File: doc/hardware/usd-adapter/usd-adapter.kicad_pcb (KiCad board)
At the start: 2 copper layers, 14.2 x 25 mm, 2 parts, among them J1 usd-plug, P1 CONN_02X04

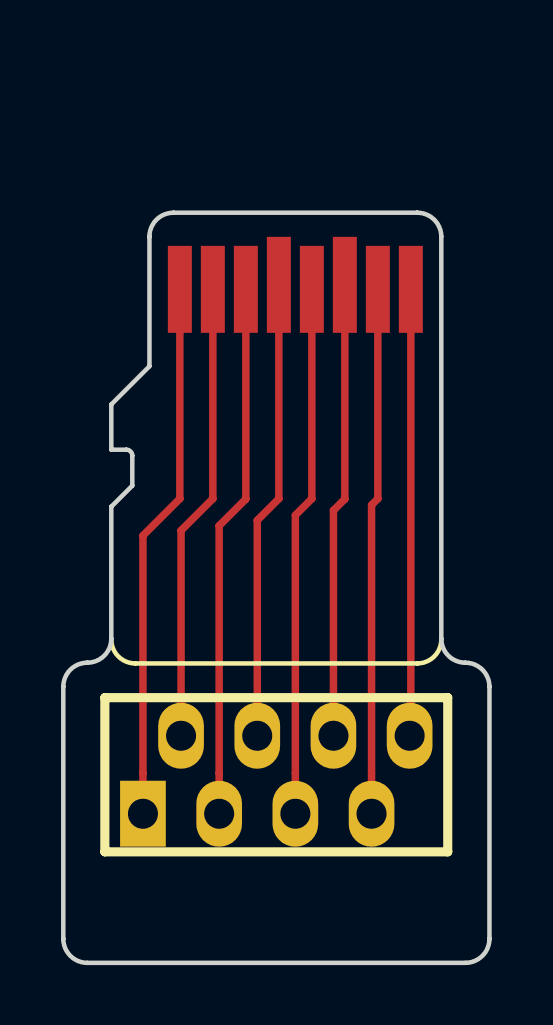
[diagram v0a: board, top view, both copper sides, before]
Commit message: Lengthen micro SD card adapter
The lengthening had to be done mainly because of boards housings.
Usually, walls of the housing caused prolems with inserting adapter
into their card socket. Now the adaper is 5mm longer.

Change-Id: I871fc60309506b883a9c277302b64e2a82f11a6e
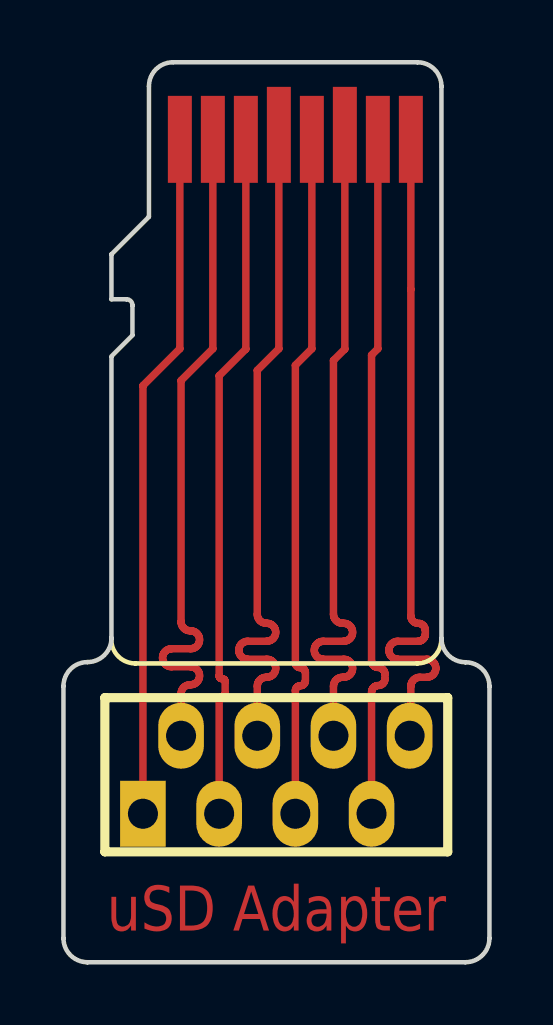
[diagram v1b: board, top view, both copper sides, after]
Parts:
- moved J1 5.00 mm to (147.3, 87.6)
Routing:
- net /N8: track 14.9 -> 23.0 mm
- net /N6: track 15.2 -> 23.0 mm
- net /N2: track 15.3 -> 23.0 mm
- net /N4: track 15.3 -> 23.0 mm
- net /N7: track 17.6 -> 23.1 mm
- net /N5: track 17.7 -> 23.1 mm
- net /N3: track 17.8 -> 23.1 mm
- net /N1: track 18.0 -> 23.0 mm
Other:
- board size 14.2 x 25 mm -> 14.2 x 30 mm
- board text added: "2. Contacts finished with gold"
- board text added: "uSD Adapter"
- board text removed: "2. Contacts coppered with gold"
